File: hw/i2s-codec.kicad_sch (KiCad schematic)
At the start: 1 part, among them IC1 TAC5212IRGER

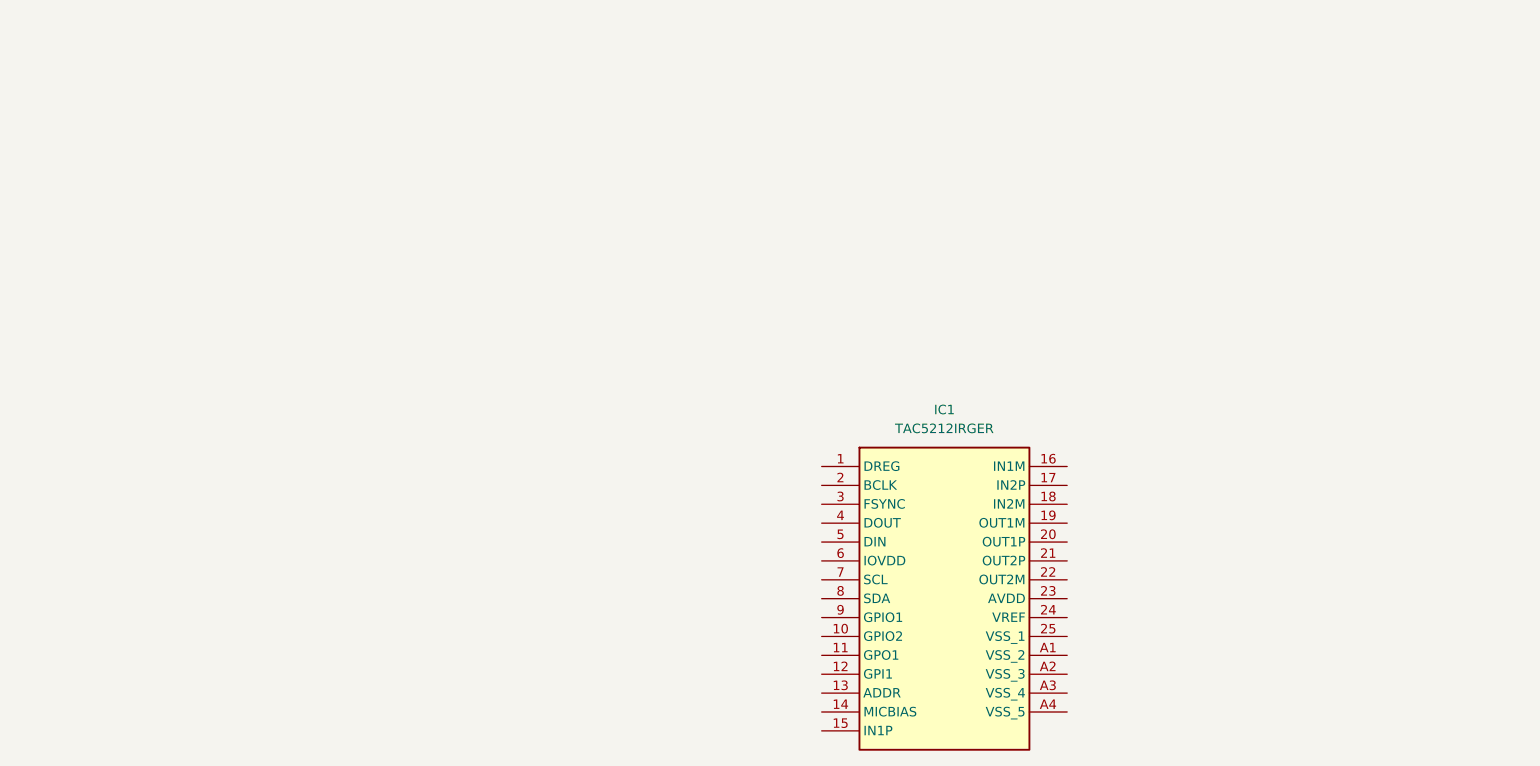
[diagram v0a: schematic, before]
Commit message: Schematic now has electret mic, exposes most connections to the IC and conditions the output lines
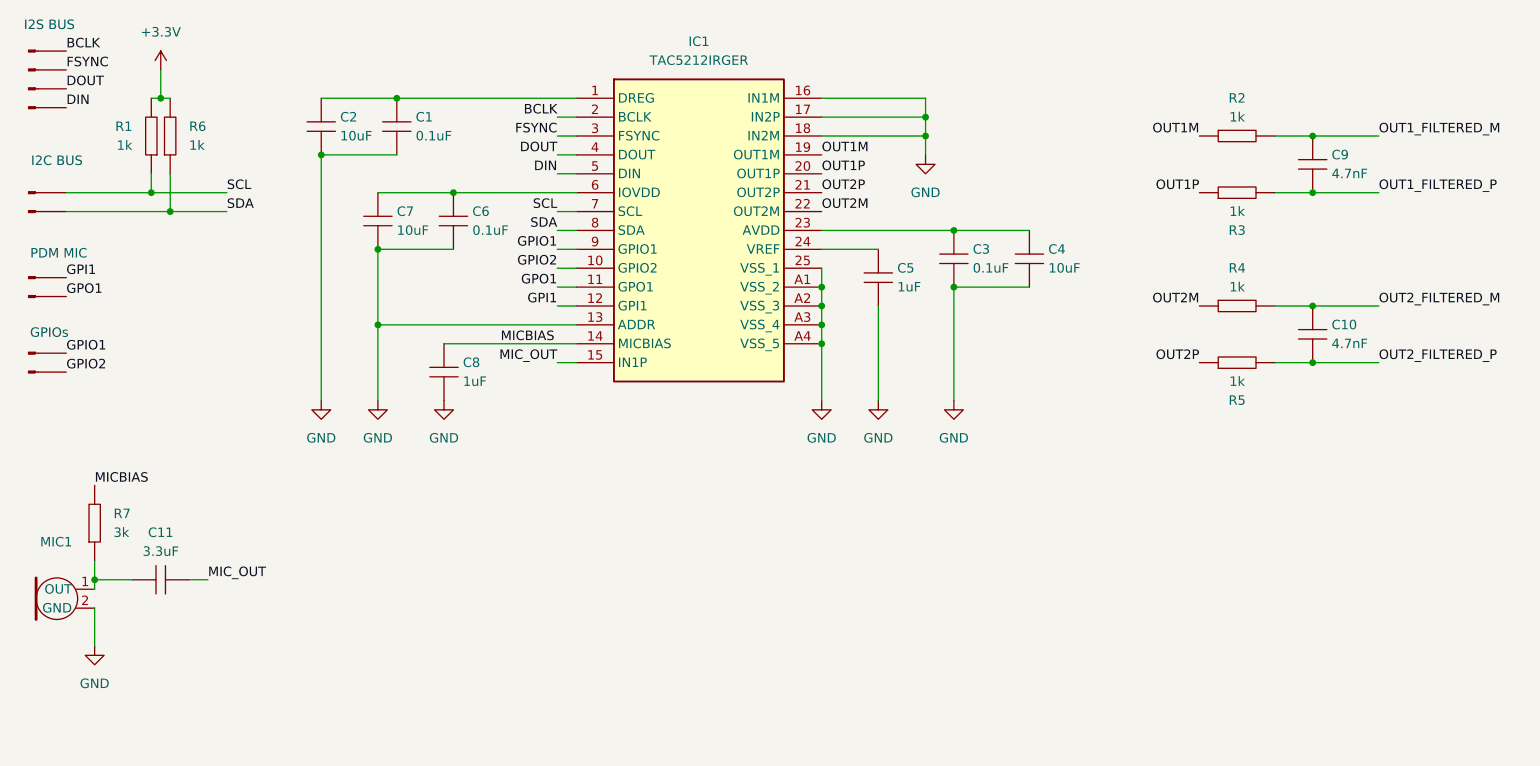
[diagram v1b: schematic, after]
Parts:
- added C1, C3, C6: 0.1uF, symbol TheCompany:C_Generic
- added C10, C9: 4.7nF, symbol TheCompany:C_Generic
- added C11: 3.3uF, symbol TheCompany:C_Generic
- added C2, C4, C7: 10uF, symbol TheCompany:C_Generic
- added C5, C8: 1uF, symbol TheCompany:C_Generic
- added J1, J10, J2, J3, J4, J5, J6, J7, J8, J9: Conn_01x01_Pin, symbol project:Conn_01x01_Pin
- added MIC1: ~, symbol TheCompany:Electret_Microphone
- added R1, R2, R3, R4, R5, R6: 1k, symbol TheCompany:R_Generic
- added R7: 3k, symbol TheCompany:R_Generic
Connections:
- net at IC1.1 (DREG): now also C1.2, C2.2
- net GPIO2: now reaches IC1.10 (GPIO2)
- net GPIO2: now also J10.1 (Pin_1)
- net GPO1: now reaches IC1.11 (GPO1)
- net GPO1: now also J8.1 (Pin_1)
- net GPI1: now reaches IC1.12 (GPI1)
- net GPI1: now also J7.1 (Pin_1)
- net GND: now reaches IC1.13 (ADDR)
- net GND: now also IC1.16 (IN1M), IC1.17 (IN2P), IC1.18 (IN2M), IC1.25 (VSS_1), IC1.A1 (VSS_2), IC1.A2 (VSS_3), IC1.A3 (VSS_4), IC1.A4 (VSS_5), C1.1, C2.1, C3.1, C4.1, C5.1, C6.1, C7.1, C8.1, MIC1.2 (GND)
- net MICBIAS: now reaches IC1.14 (MICBIAS)
- net MICBIAS: now also C8.2, R7.2
- net MIC_OUT: now reaches IC1.15 (IN1P)
- net MIC_OUT: now also C11.2
- net OUT1M: now reaches IC1.19 (OUT1M)
- net OUT1M: now also R2.1
- net BCLK: now reaches IC1.2 (BCLK)
- net BCLK: now also J5.1 (Pin_1)
- net OUT1P: now reaches IC1.20 (OUT1P)
- net OUT1P: now also R3.1
- net OUT2P: now reaches IC1.21 (OUT2P)
- net OUT2P: now also R5.1
- net OUT2M: now reaches IC1.22 (OUT2M)
- net OUT2M: now also R4.1
- net at IC1.23 (AVDD): now also C3.2, C4.2
- net at IC1.24 (VREF): now also C5.2
- net FSYNC: now reaches IC1.3 (FSYNC)
- net FSYNC: now also J1.1 (Pin_1)
- net DOUT: now reaches IC1.4 (DOUT)
- net DOUT: now also J2.1 (Pin_1)
- net DIN: now reaches IC1.5 (DIN)
- net DIN: now also J3.1 (Pin_1)
- net at IC1.6 (IOVDD): now also C6.2, C7.2
- net SCL: now reaches IC1.7 (SCL)
- net SCL: now also J4.1 (Pin_1), R1.1
- net SDA: now reaches IC1.8 (SDA)
- net SDA: now also J6.1 (Pin_1), R6.1
- net GPIO1: now reaches IC1.9 (GPIO1)
- net GPIO1: now also J9.1 (Pin_1)
- new net: C11.1, MIC1.1 (OUT), R7.1
- new net +3.3V: R1.2, R6.2
- new net OUT1_FILTERED_M: C9.2, R2.2
- new net OUT1_FILTERED_P: C9.1, R3.2
- new net OUT2_FILTERED_M: C10.2, R4.2
- new net OUT2_FILTERED_P: C10.1, R5.2
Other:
- note added: "GPIOs"
- note added: "I2C BUS"
- note added: "I2S BUS"
- note added: "PDM MIC"
- moved on the sheet: IC1
